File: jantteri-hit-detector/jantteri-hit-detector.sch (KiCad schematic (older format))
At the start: 35 parts, among them J1 SWD, J2 main_connector, J3 DBG_PORT, J4 LED_PORT, Q1 Si2319CDS, U1 STM32G030C8T6, U2 AMS1117-3.3, U3 KX023, U4 TXB0104RUT, U5 KX023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

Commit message: remove hit-detector i2c pullup resistors
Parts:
- removed J2: main_connector, Connector_JST2:JST_ZH_B5B-ZR_1x05_P1.50mm_Vertical, symbol Connector:Conn_01x05_Male
- removed J4: LED_PORT, Connector_JST2:JST_ZH_B3B-ZR_1x03_P1.50mm_Vertical, symbol Connector:Conn_01x03_Male
- removed R4, R5: 4K7, Resistor_SMD:R_0402_1005Metric, symbol Device:R_Small
- added J2: Conn_01x06_Male, Connector_JST2:JST_ZH_B6B-ZR_1x06_P1.50mm_Vertical, symbol Connector:Conn_01x06_Male
- added J4: Conn_01x04_Male, Connector_JST2:JST_ZH_B4B-ZR_1x04_P1.50mm_Vertical, symbol Connector:Conn_01x04_Male
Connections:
- net labels added: +12V
- wire segments 91 -> 88
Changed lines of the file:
@@
 	1    0    0    -1
-$EndComp
-$Comp
-L Connector:Conn_01x03_Male J4
-U 1 1 611644A0
-P 9050 3650
-F 0 "J4" H 9158 3931 50  0000 C CNN
-F 1 "LED_PORT" H 9158 3840 50  0000 C CNN
-F 2 "Connector_JST2:JST_ZH_B3B-ZR_1x03_P1.50mm_Vertical" H 9050 3650 50  0001 C CNN
-F 3 "~" H 9050 3650 50  0001 C CNN
-	1    9050 3650
-	-1   0    0    1
 $EndComp
 Text GLabel 6750 3500 0    50   Input ~ 0
@@
 Text GLabel 7550 3500 2    50   Input ~ 0
 LED_DATA_5V
-Text GLabel 8850 3650 0    50   Input ~ 0
+Text GLabel 9100 3650 0    50   Input ~ 0
 LED_DATA_5V
-$Comp
-L power:+5V #PWR034
-U 1 1 6116AE43
-P 8600 3550
-F 0 "#PWR034" H 8600 3400 50  0001 C CNN
-F 1 "+5V" H 8615 3723 50  0000 C CNN
-F 2 "" H 8600 3550 50  0001 C CNN
-F 3 "" H 8600 3550 50  0001 C CNN
-	1    8600 3550
-	1    0    0    -1
-$EndComp
 $Comp
 L power:GND #PWR028
@@
 L power:GND #PWR035
 U 1 1 61170746
-P 8600 3750
-F 0 "#PWR035" H 8600 3500 50  0001 C CNN
-F 1 "GND" H 8605 3577 50  0000 C CNN
-F 2 "" H 8600 3750 50  0001 C CNN
-F 3 "" H 8600 3750 50  0001 C CNN
-	1    8600 3750
-	1    0    0    -1
-$EndComp
-Wire Wire Line
-	8850 3750 8600 3750
+P 9100 3450
+F 0 "#PWR035" H 9100 3200 50  0001 C CNN
+F 1 "GND" V 9105 3322 50  0000 R CNN
+F 2 "" H 9100 3450 50  0001 C CNN
+F 3 "" H 9100 3450 50  0001 C CNN
+	1    9100 3450
+	0    1    1    0
+$EndComp
 NoConn ~ 6750 3700
 NoConn ~ 6750 3900
@@
 NoConn ~ 7550 3900
 NoConn ~ 7550 3700
-Wire Wire Line
-	8600 3550 8850 3550
 $Comp
 L Device:C_Small C13
@@
 Wire Notes Line
 	4950 4750 11200 4750
-$Comp
-L Connector:Conn_01x05_Male J2
-U 1 1 611B5CE8
-P 5550 5600
-F 0 "J2" H 5650 6050 50  0000 C CNN
-F 1 "main_connector" H 5650 5950 50  0000 C CNN
-F 2 "Connector_JST2:JST_ZH_B5B-ZR_1x05_P1.50mm_Vertical" H 5550 5600 50  0001 C CNN
-F 3 "~" H 5550 5600 50  0001 C CNN
-	1    5550 5600
-	1    0    0    -1
-$EndComp
 Wire Wire Line
 	5750 5400 6250 5400
 Wire Wire Line
 	5750 5800 6250 5800
-$Comp
-L Device:R_Small R5
-U 1 1 611C18B3
-P 7000 5700
-F 0 "R5" H 7100 5700 50  0000 L CNN
-F 1 "4K7" H 7100 5600 50  0000 L CNN
-F 2 "Resistor_SMD:R_0402_1005Metric" H 7000 5700 50  0001 C CNN
-F 3 "~" H 7000 5700 50  0001 C CNN
-F 4 "C25900" H 7000 5700 50  0001 C CNN "LCSC"
-	1    7000 5700
-	1    0    0    -1
-$EndComp
-$Comp
-L Device:R_Small R4
-U 1 1 611C2304
-P 6550 5800
-F 0 "R4" H 6650 5800 50  0000 L CNN
-F 1 "4K7" H 6650 5700 50  0000 L CNN
-F 2 "Resistor_SMD:R_0402_1005Metric" H 6550 5800 50  0001 C CNN
-F 3 "~" H 6550 5800 50  0001 C CNN
-F 4 "C25900" H 6550 5800 50  0001 C CNN "LCSC"
-	1    6550 5800
-	1    0    0    -1
-$EndComp
-$Comp
-L power:GND #PWR023
-U 1 1 611C4B2C
-P 6550 5900
-F 0 "#PWR023" H 6550 5650 50  0001 C CNN
-F 1 "GND" H 6555 5727 50  0000 C CNN
-F 2 "" H 6550 5900 50  0001 C CNN
-F 3 "" H 6550 5900 50  0001 C CNN
-	1    6550 5900
-	1    0    0    -1
-$EndComp
-$Comp
-L power:GND #PWR026
-U 1 1 611C4DEE
-P 7000 5800
-F 0 "#PWR026" H 7000 5550 50  0001 C CNN
-F 1 "GND" H 7005 5627 50  0000 C CNN
-F 2 "" H 7000 5800 50  0001 C CNN
-F 3 "" H 7000 5800 50  0001 C CNN
-	1    7000 5800
-	1    0    0    -1
-$EndComp
-Wire Wire Line
-	5750 5700 6550 5700
-Wire Wire Line
-	5750 5600 7000 5600
 Text GLabel 5750 5500 2    50   Input ~ 0
 HIT_INT
@@
 Text GLabel 7050 5600 2    50   Input ~ 0
 HIT_SCL
-Wire Wire Line
-	7050 5600 7000 5600
-Connection ~ 7000 5600
-Wire Wire Line
-	6600 5700 6550 5700
-Connection ~ 6550 5700
 Text GLabel 4100 6500 2    50   Input ~ 0
 HIT_SDA
@@
 NoConn ~ 2600 4150
 NoConn ~ 2600 4250
-$Comp
-L power:VDC #PWR020
-U 1 1 611E2A1D
-P 6250 5400
-F 0 "#PWR020" H 6250 5300 50  0001 C CNN
-F 1 "VDC" H 6265 5573 50  0000 C CNN
-F 2 "" H 6250 5400 50  0001 C CNN
-F 3 "" H 6250 5400 50  0001 C CNN
-	1    6250 5400
-	1    0    0    -1
-$EndComp
 $Comp
 L power:VDC #PWR06
@@
 Text GLabel 4100 3950 2    50   Input ~ 0
 KX3_TRIG
+$Comp
+L Connector:Conn_01x06_Male J2
+U 1 1 612C7431
+P 5550 5500
+F 0 "J2" H 5658 5881 50  0000 C CNN
+F 1 "Conn_01x06_Male" H 5658 5790 50  0000 C CNN
+F 2 "Connector_JST2:JST_ZH_B6B-ZR_1x06_P1.50mm_Vertical" H 5550 5500 50  0001 C CNN
+F 3 "~" H 5550 5500 50  0001 C CNN
+	1    5550 5500
+	1    0    0    -1
+$EndComp
+$Comp
+L power:+12V #PWR0101
+U 1 1 612C9C64
+P 6100 5300
+F 0 "#PWR0101" H 6100 5150 50  0001 C CNN
+F 1 "+12V" H 6115 5473 50  0000 C CNN
+F 2 "" H 6100 5300 50  0001 C CNN
+F 3 "" H 6100 5300 50  0001 C CNN
+	1    6100 5300
+	1    0    0    -1
+$EndComp
+Wire Wire Line
+	5750 5300 6100 5300
+$Comp
+L power:VDC #PWR0102
+U 1 1 612CD1D4
+P 6250 5400
+F 0 "#PWR0102" H 6250 5300 50  0001 C CNN
+F 1 "VDC" H 6265 5573 50  0000 C CNN
+F 2 "" H 6250 5400 50  0001 C CNN
+F 3 "" H 6250 5400 50  0001 C CNN
+	1    6250 5400
+	1    0    0    -1
+$EndComp
+$Comp
+L power:+12V #PWR0103
+U 1 1 612CE009
+P 9100 3350
+F 0 "#PWR0103" H 9100 3200 50  0001 C CNN
+F 1 "+12V" H 9115 3523 50  0000 C CNN
+F 2 "" H 9100 3350 50  0001 C CNN
+F 3 "" H 9100 3350 50  0001 C CNN
+	1    9100 3350
+	1    0    0    -1
+$EndComp
+$Comp
+L Connector:Conn_01x04_Male J4
+U 1 1 612D060B
+P 9300 3550
+F 0 "J4" H 9272 3432 50  0000 R CNN
+F 1 "Conn_01x04_Male" H 9272 3523 50  0000 R CNN
+F 2 "Connector_JST2:JST_ZH_B4B-ZR_1x04_P1.50mm_Vertical" H 9300 3550 50  0001 C CNN
+F 3 "~" H 9300 3550 50  0001 C CNN
+	1    9300 3550
+	-1   0    0    1
+$EndComp
+$Comp
+L power:GND #PWR0104
+U 1 1 612D6CFA
+P 9100 3550
+F 0 "#PWR0104" H 9100 3300 50  0001 C CNN
+F 1 "GND" V 9105 3422 50  0000 R CNN
+F 2 "" H 9100 3550 50  0001 C CNN
+F 3 "" H 9100 3550 50  0001 C CNN
+	1    9100 3550
+	0    1    1    0
+$EndComp
+Wire Wire Line
+	5750 5700 6600 5700
+Wire Wire Line
+	5750 5600 7050 5600
 $EndSCHEMATC

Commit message: hit-detector update
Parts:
- removed C1: 4u7, Capacitor_SMD:C_1206_3216Metric, symbol Device:C_Small
- removed C10, C8: 10u, Capacitor_SMD:C_0805_2012Metric, symbol Device:C_Small
- removed C11, C12, C13, C14, C15, C16, C17, C18, C2, C3, C4: 100n, Capacitor_SMD:C_0603_1608Metric, symbol Device:C_Small
- removed C7, C9: 12p, Capacitor_SMD:C_0402_1005Metric, symbol Device:C_Small
- removed D1: LED, LED_SMD:LED_0603_1608Metric, symbol Device:LED
- removed J1: SWD, Connector_PinHeader_1.27mm:PinHeader_2x05_P1.27mm_Vertical_SMD, symbol Connector_Generic:Conn_02x05_Odd_Even
- removed J3: DBG_PORT, Connector_JST2:JST_ZH_B3B-ZR_1x03_P1.50mm_Vertical, symbol Connector:Conn_01x03_Male
- removed J4: Conn_01x04_Male, Connector_JST2:JST_ZH_B4B-ZR_1x04_P1.50mm_Vertical, symbol Connector:Conn_01x04_Male
- removed Q1: Si2319CDS, Package_TO_SOT_SMD:SOT-23, symbol Transistor_FET:Si2319CDS
- removed R1: 1k5, Resistor_SMD:R_0402_1005Metric, symbol Device:R_Small
- removed R2: 47, Resistor_SMD:R_0402_1005Metric, symbol Device:R_Small
- removed R3: 100K, Resistor_SMD:R_0402_1005Metric, symbol Device:R_Small
- removed U1: STM32G030C8T6, Package_QFP:LQFP-48_7x7mm_P0.5mm, symbol STM32G030C8T6:STM32G030C8T6
- removed U2: AMS1117-3.3, Package_TO_SOT_SMD:SOT-223-3_TabPin2, symbol Regulator_Linear:AMS1117-3.3
- removed U3, U5, U6: KX023, Package_LGA:LGA-16_3x3mm_P0.5mm_LayoutBorder3x5y, symbol JLC_assembled:KX023
- removed U4: TXB0104RUT, Package_DFN_QFN:Texas_R_PUQFN-N12, symbol Logic_LevelTranslator:TXB0104RUT
- removed Y1: 16MHz, Crystal:Crystal_SMD_3225-4Pin_3.2x2.5mm, symbol Device:Crystal_GND24_Small
- renumbered J2 to J1
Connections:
- net labels added: USB-5V, VCC
- net labels removed: DBG_RX, DBG_TX, HSE_IN, HSE_OUT, LED_DATA_5V, NRST, STATUS_LED, SWCLK, SWDIO, SWO, VDC
- wire segments 88 -> 38
- no-connect marks 11 -> 2
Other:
- note removed: "3.3V supply"
- note removed: "Cload = 2 * ( Cl - Cstary )"
- note removed: "STM32"
- note removed: "programmer connection"
- moved on the sheet: FB1, J1

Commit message: jantteri-pwr-motor
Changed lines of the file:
@@
 Wire Wire Line
 	2250 3000 2300 3000
+$Comp
+L power:GND #PWR?
+U 1 1 611C08D9
+P 1000 4850
+F 0 "#PWR?" H 1000 4600 50  0001 C CNN
+F 1 "GND" H 1005 4677 50  0000 C CNN
+F 2 "" H 1000 4850 50  0001 C CNN
+F 3 "" H 1000 4850 50  0001 C CNN
+	1    1000 4850
+	1    0    0    -1
+$EndComp
+Wire Wire Line
+	1200 4850 1000 4850
 $EndSCHEMATC

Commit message: random changes
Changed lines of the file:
@@
 Wire Notes Line
 	4950 500  4950 7800
-Text GLabel 5700 1800 0    50   Input ~ 0
-KX1_TRIG
 Text GLabel 5700 1900 0    50   Input ~ 0
 KX1_INT1
@@
 Text GLabel 6400 1550 2    50   Input ~ 0
 KX1_CS
-Text GLabel 7550 1800 0    50   Input ~ 0
-KX2_TRIG
 Text GLabel 7550 1900 0    50   Input ~ 0
 KX2_INT1
@@
 F5 "EN" I L 1100 1100 50
 $EndSheet
-$Sheet
-S 5700 1450 700  650
-U 611EAD56
-F0 "KX023" 50
-F1 "KX023.sch" 50
-F2 "GND" I L 5700 1600 50
-F3 "3V3" I L 5700 1500 50
-F4 "CS" I R 6400 1550 50
-F5 "SCLK" I R 6400 1650 50
-F6 "MOSI" I R 6400 1750 50
-F7 "MISO" I R 6400 1850 50
-F8 "TRIG" I L 5700 1800 50
-F9 "INT1" I L 5700 1900 50
-F10 "INT2" I L 5700 2000 50
-$EndSheet
-$Sheet
-S 7550 1450 700  650
-U 611F79B1
-F0 "sheet611F799F" 50
-F1 "KX023.sch" 50
-F2 "GND" I L 7550 1600 50
-F3 "3V3" I L 7550 1500 50
-F4 "CS" I R 8250 1550 50
-F5 "SCLK" I R 8250 1650 50
-F6 "MOSI" I R 8250 1750 50
-F7 "MISO" I R 8250 1850 50
-F8 "TRIG" I L 7550 1800 50
-F9 "INT1" I L 7550 1900 50
-F10 "INT2" I L 7550 2000 50
-$EndSheet
 $Comp
 L power:+3.3V #PWR06
@@
 	1    0    0    -1
 $EndComp
-$Sheet
-S 9500 1450 700  650
-U 611F8F80
-F0 "sheet611F8F6E" 50
-F1 "KX023.sch" 50
-F2 "GND" I L 9500 1600 50
-F3 "3V3" I L 9500 1500 50
-F4 "CS" I R 10200 1550 50
-F5 "SCLK" I R 10200 1650 50
-F6 "MOSI" I R 10200 1750 50
-F7 "MISO" I R 10200 1850 50
-F8 "TRIG" I L 9500 1800 50
-F9 "INT1" I L 9500 1900 50
-F10 "INT2" I L 9500 2000 50
-$EndSheet
 Text GLabel 10200 1650 2    50   Input ~ 0
 KX_SCLK
@@
 Text GLabel 8250 1650 2    50   Input ~ 0
 KX_SCLK
-Text GLabel 9500 1800 0    50   Input ~ 0
-KX3_TRIG
 Text GLabel 9500 1900 0    50   Input ~ 0
 KX3_INT1
@@
 Text GLabel 3650 4300 2    50   Input ~ 0
 HIT_INT
-Text GLabel 3650 4450 2    50   Input ~ 0
-KX1_TRIG
 Text GLabel 3650 3250 2    50   Input ~ 0
 KX1_INT1
-Text GLabel 3650 3350 2    50   Input ~ 0
-KX1_INT2
 Text GLabel 3650 4550 2    50   Input ~ 0
 KX1_CS
 Text GLabel 3650 3450 2    50   Input ~ 0
-KX2_TRIG
-Text GLabel 3650 3550 2    50   Input ~ 0
 KX2_INT1
-Text GLabel 3650 4650 2    50   Input ~ 0
-KX2_INT2
 Text GLabel 3650 4750 2    50   Input ~ 0
 KX2_CS
-Text GLabel 3650 4850 2    50   Input ~ 0
-KX3_TRIG
 Text GLabel 3650 3650 2    50   Input ~ 0
 KX3_INT1
@@
 KX3_CS
 $Comp
-L power:+3.3V #PWR?
+L power:+3.3V #PWR0101
 U 1 1 6127D06C
 P 2100 2900
-F 0 "#PWR?" H 2100 2750 50  0001 C CNN
+F 0 "#PWR0101" H 2100 2750 50  0001 C CNN
 F 1 "+3.3V" H 2115 3073 50  0000 C CNN
 F 2 "" H 2100 2900 50  0001 C CNN
@@
 	2300 2900 2100 2900
 $Comp
-L power:GND #PWR?
+L power:GND #PWR0102
 U 1 1 6127E179
 P 2100 2950
-F 0 "#PWR?" H 2100 2700 50  0001 C CNN
+F 0 "#PWR0102" H 2100 2700 50  0001 C CNN
 F 1 "GND" H 2105 2777 50  0000 C CNN
 F 2 "" H 2100 2950 50  0001 C CNN
@@
 	2250 3000 2300 3000
 $Comp
-L power:GND #PWR?
+L power:GND #PWR0103
 U 1 1 611C08D9
 P 1000 4850
-F 0 "#PWR?" H 1000 4600 50  0001 C CNN
+F 0 "#PWR0103" H 1000 4600 50  0001 C CNN
 F 1 "GND" H 1005 4677 50  0000 C CNN
 F 2 "" H 1000 4850 50  0001 C CNN
@@
 Wire Wire Line
 	1200 4850 1000 4850
+$Sheet
+S 5700 1450 700  600
+U 6154A631
+F0 "LIS2DW12" 50
+F1 "LIS2DW12.sch" 50
+F2 "GND" I L 5700 1600 50
+F3 "3V3" I L 5700 1500 50
+F4 "CS" I R 6400 1550 50
+F5 "SCLK" I R 6400 1650 50
+F6 "MOSI" I R 6400 1750 50
+F7 "MISO" I R 6400 1850 50
+F8 "INT1" I L 5700 1900 50
+F9 "INT2" I L 5700 2000 50
+$EndSheet
+$Sheet
+S 7550 1450 700  600
+U 615681DE
+F0 "sheet615681C0" 50
+F1 "LIS2DW12.sch" 50
+F2 "GND" I L 7550 1600 50
+F3 "3V3" I L 7550 1500 50
+F4 "CS" I R 8250 1550 50
+F5 "SCLK" I R 8250 1650 50
+F6 "MOSI" I R 8250 1750 50
+F7 "MISO" I R 8250 1850 50
+F8 "INT1" I L 7550 1900 50
+F9 "INT2" I L 7550 2000 50
+$EndSheet
+Text GLabel 3650 4650 2    50   Input ~ 0
+KX2_INT2
+$Sheet
+S 9500 1450 700  600
+U 6156935E
+F0 "sheet61569340" 50
+F1 "LIS2DW12.sch" 50
+F2 "GND" I L 9500 1600 50
+F3 "3V3" I L 9500 1500 50
+F4 "CS" I R 10200 1550 50
+F5 "SCLK" I R 10200 1650 50
+F6 "MOSI" I R 10200 1750 50
+F7 "MISO" I R 10200 1850 50
+F8 "INT1" I L 9500 1900 50
+F9 "INT2" I L 9500 2000 50
+$EndSheet
+Text GLabel 3650 3350 2    50   Input ~ 0
+KX1_INT2
 $EndSCHEMATC

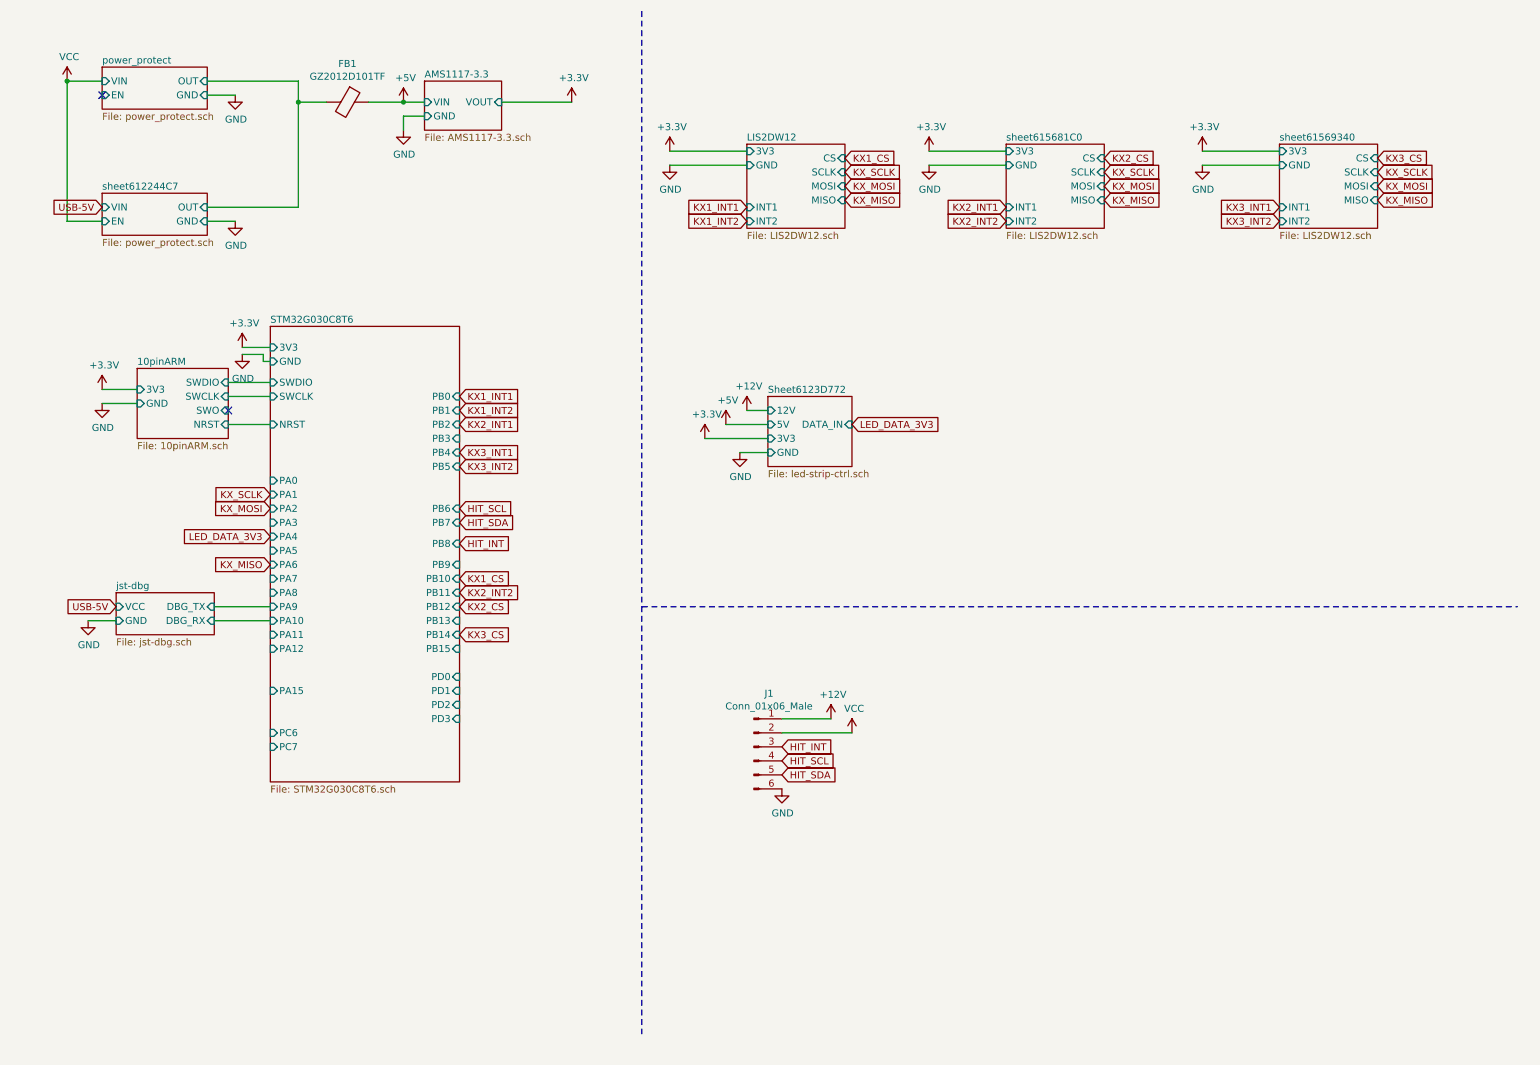
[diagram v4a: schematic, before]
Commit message: Tuubijantteri design Ordered
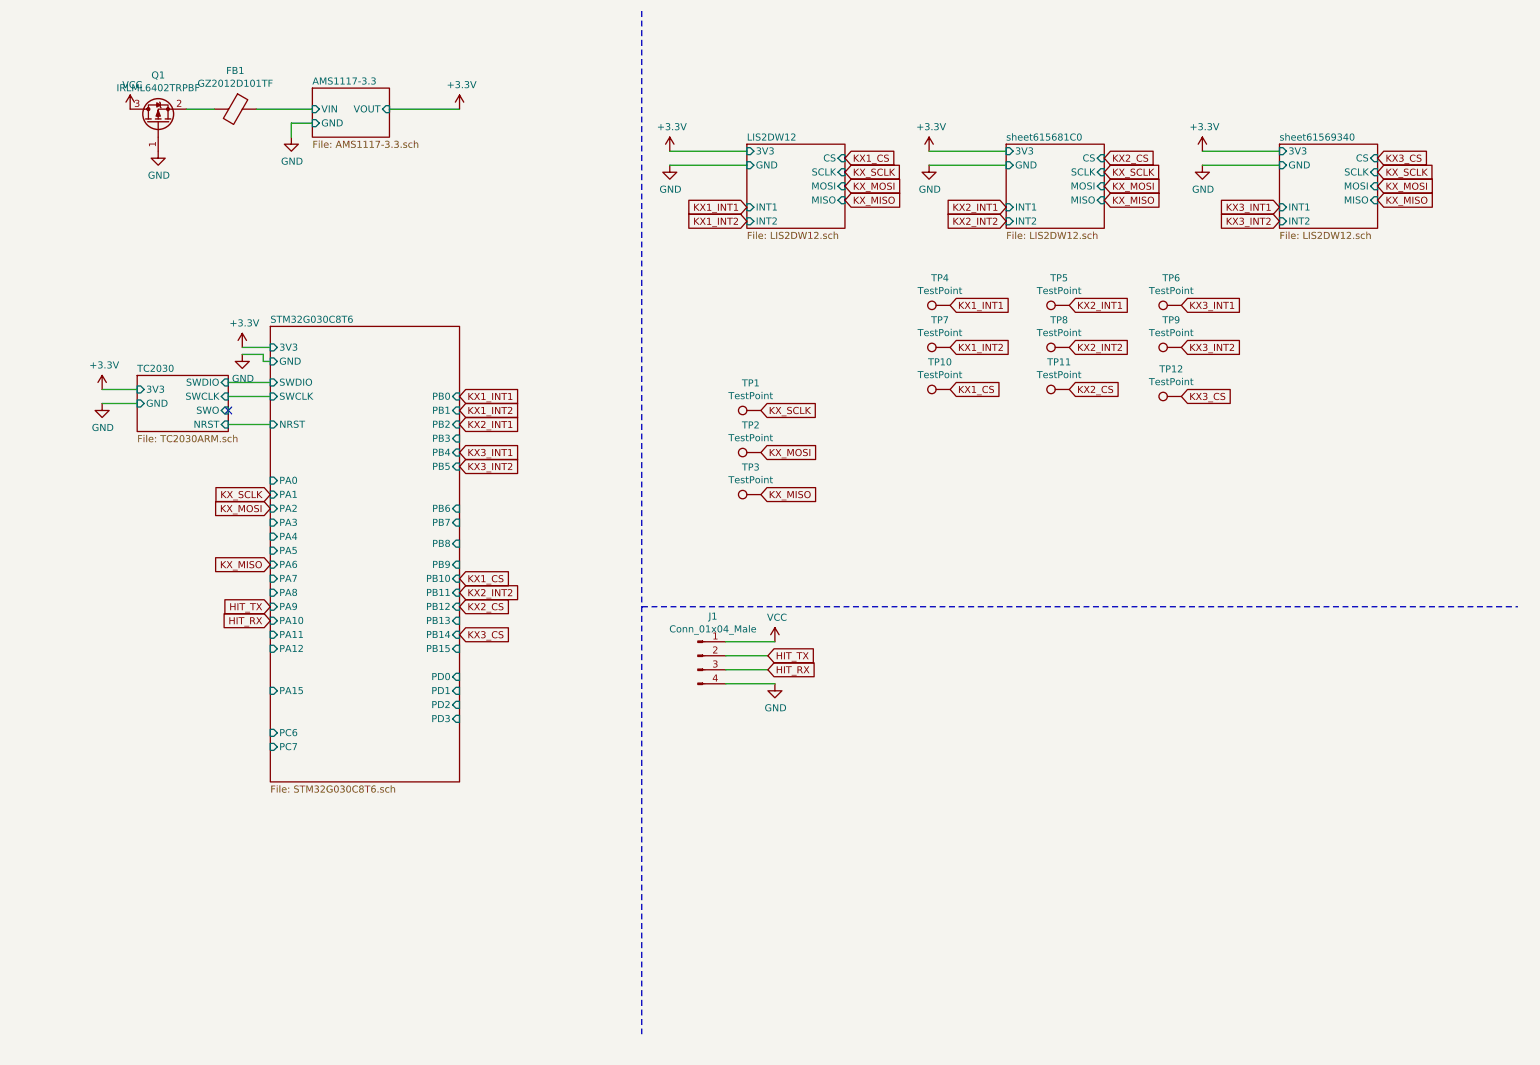
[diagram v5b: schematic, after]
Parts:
- removed J1: Conn_01x06_Male, Connector_JST2:JST_ZH_B6B-ZR_1x06_P1.50mm_Vertical, symbol Connector:Conn_01x06_Male
- added J1: Conn_01x04_Male, Connector_JST2:JST_ZH_B4B-ZR_1x04_P1.50mm_Vertical, symbol Connector:Conn_01x04_Male
- added Q1: IRLML6402TRPBF, Package_TO_SOT_SMD:SOT-23, symbol Transistor_FET:Si2319CDS
- added TP1, TP10, TP11, TP12, TP2, TP3, TP4, TP5, TP6, TP7, TP8, TP9: TestPoint, TestPoint:TestPoint_Pad_D1.0mm, symbol Connector:TestPoint
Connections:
- net GND: now also J1.4 (Pin_4), Q1.1 (G)
- net KX1_CS: now also TP10.1
- net KX1_INT1: now also TP4.1
- net KX1_INT2: now also TP7.1
- net KX2_CS: now also TP11.1
- net KX2_INT1: now also TP5.1
- net KX2_INT2: now also TP8.1
- net KX3_CS: now also TP12.1
- net KX3_INT1: now also TP6.1
- net KX3_INT2: now also TP9.1
- net KX_MISO: now also TP3.1
- net KX_MOSI: now also TP2.1
- net KX_SCLK: now also TP1.1
- net VCC: now also J1.1 (Pin_1), Q1.3 (D)
- net +5V renamed AMS1117-3.3/VIN
- net power_protect/OUT: no longer names the net of FB1.2
- net power_protect/OUT: now also Q1.2 (S)
- new net HIT_RX: J1.3 (Pin_3)
- new net HIT_TX: J1.2 (Pin_2)
- no-connect marks 2 -> 1
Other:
- moved on the sheet: FB1
